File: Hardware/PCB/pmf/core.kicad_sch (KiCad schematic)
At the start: 44 parts, among them U1 AS3320, U2 TL072

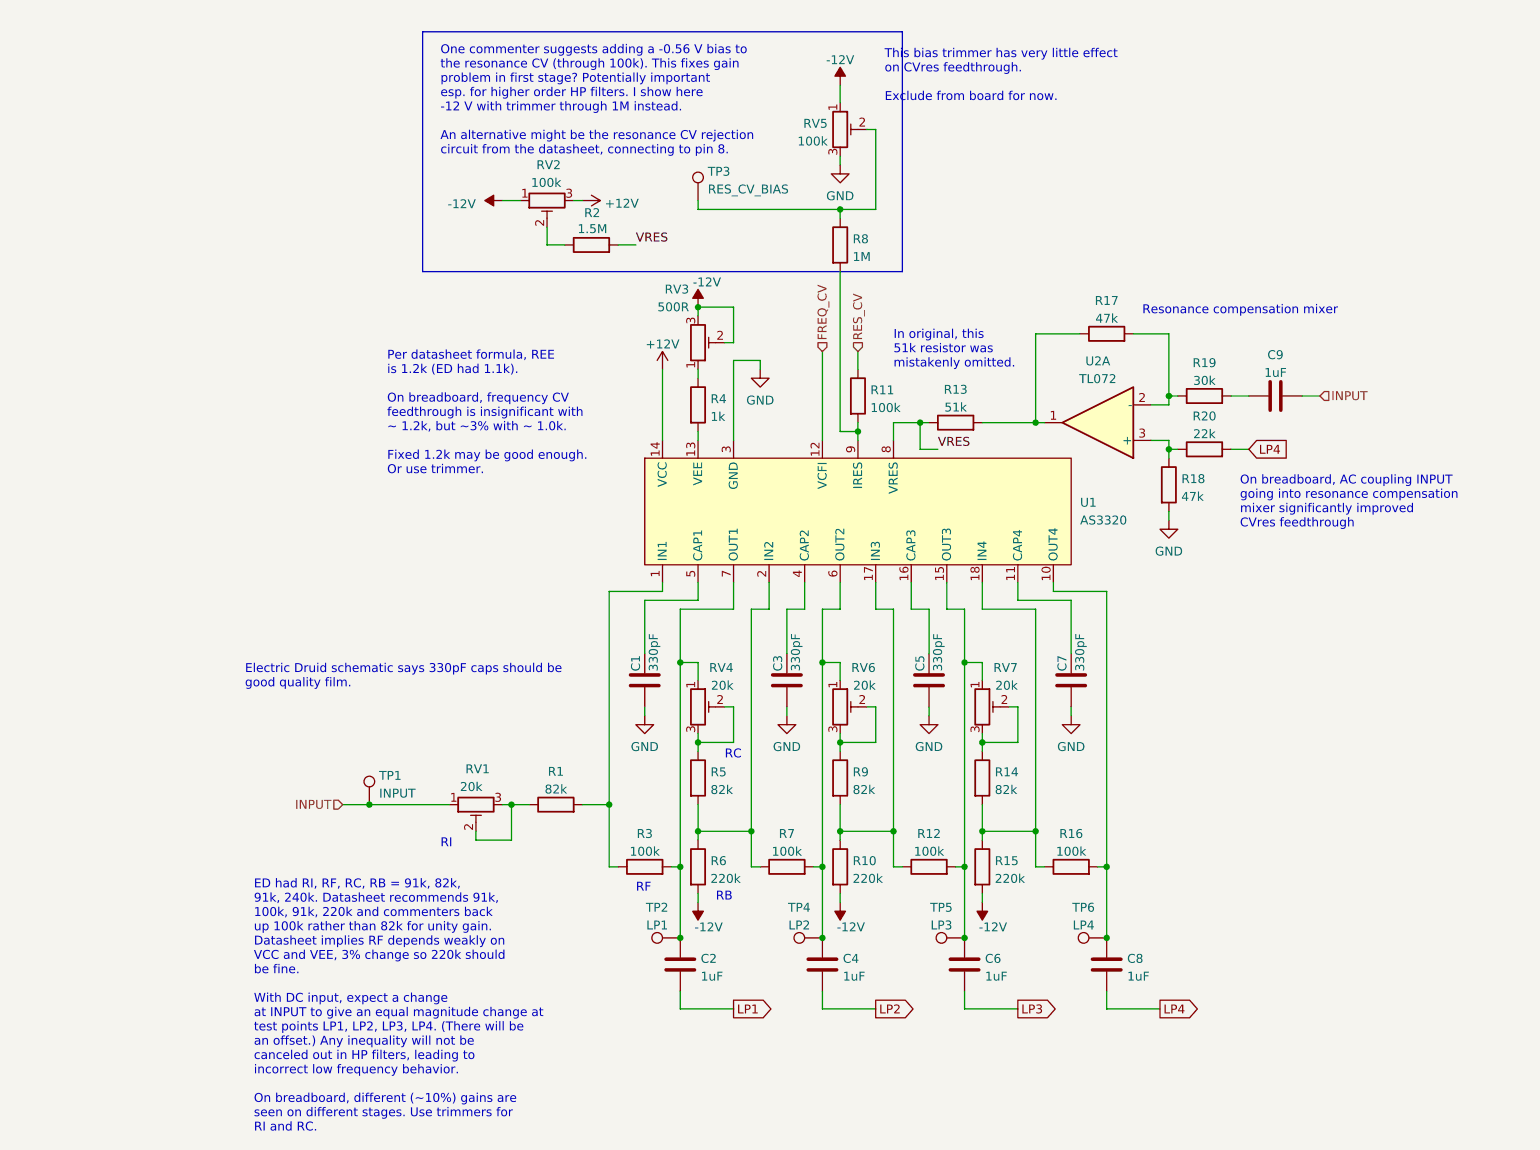
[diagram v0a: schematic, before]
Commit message: Reorganize filter core schematic
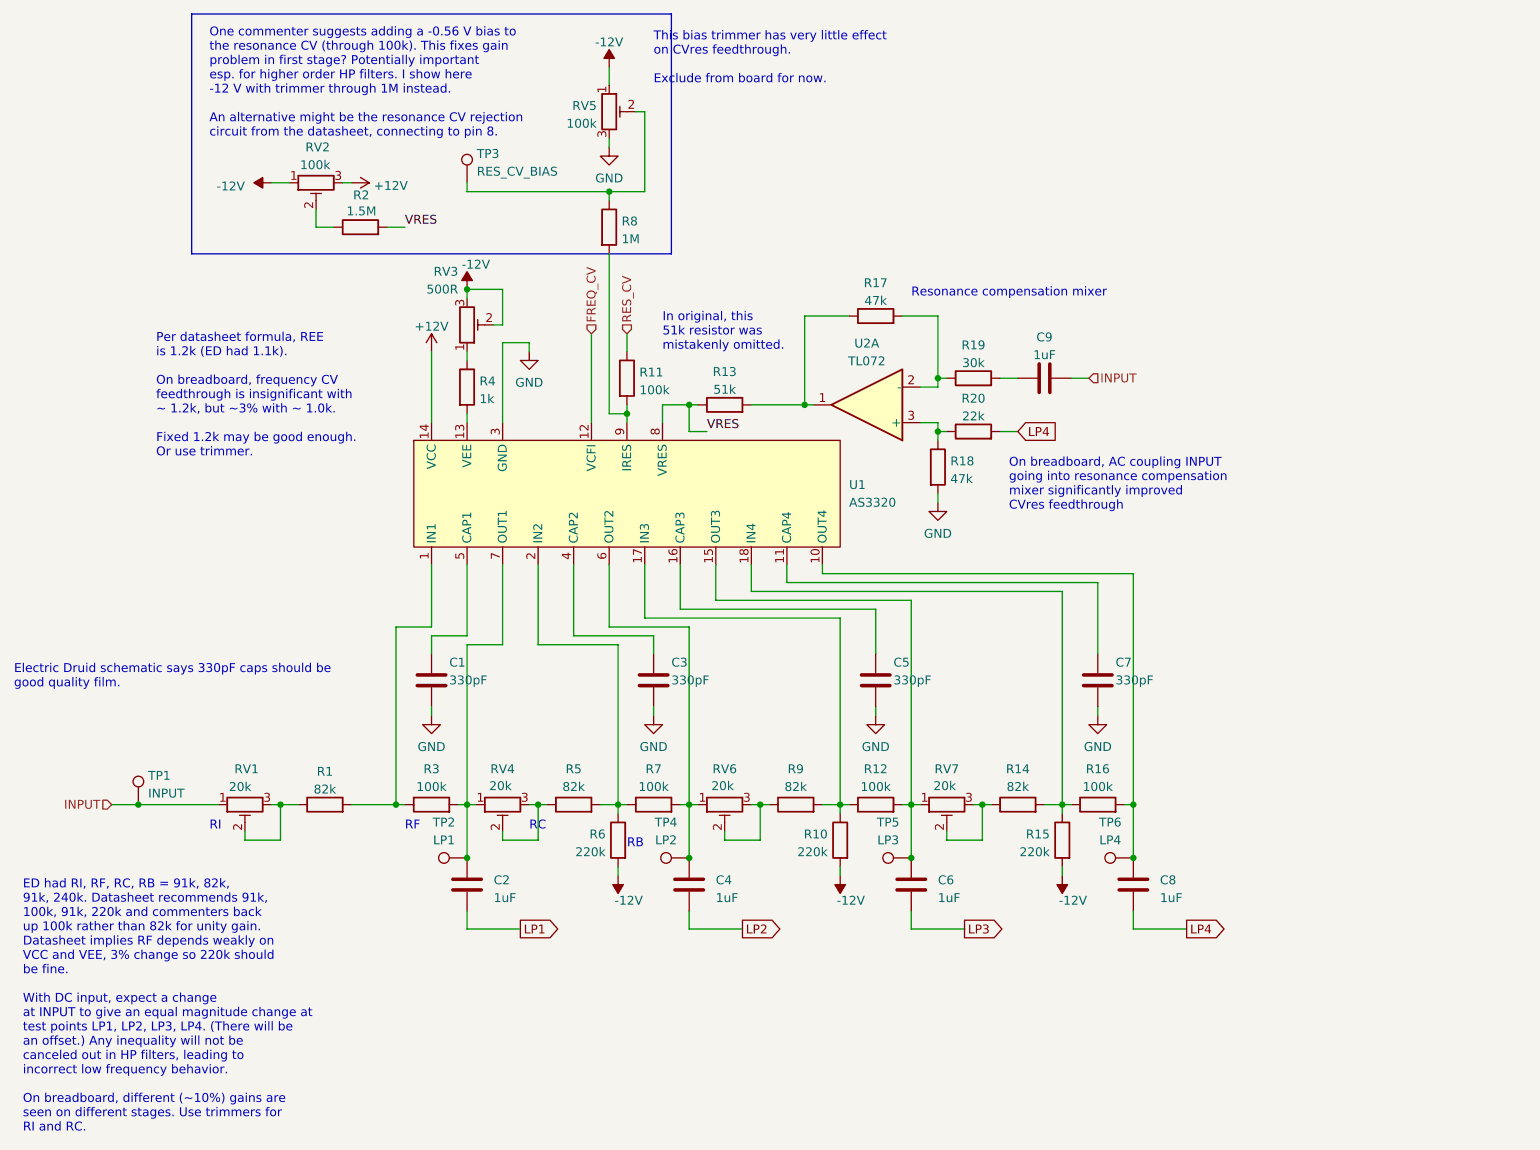
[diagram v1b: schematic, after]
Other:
- moved on the sheet: C1, C9, R1, R11, R13, R17, R18, R19, R2, R20, R4, R8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

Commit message: Rename libraries
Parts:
- C1, C3, C5, C7: footprint ao_tht:C_Rect_L7.2mm_W2.5mm_P5.00mm_FKS2_FKP2_MKS2_MKP2 -> AO_tht:C_Rect_L7.2mm_W2.5mm_P5.00mm_FKS2_FKP2_MKS2_MKP2; symbol ao_symbols:C -> AO_symbols:C
- C2, C4, C6, C8, C9: footprint ao_tht:C_Rect_L7.2mm_W7.2mm_P5.00mm_FKS2_FKP2_MKS2_MKP2 -> AO_tht:C_Rect_L7.2mm_W7.2mm_P5.00mm_FKS2_FKP2_MKS2_MKP2; symbol ao_symbols:C -> AO_symbols:C
- R1, R10, R11, R12, R13, R14, R15, R16, R17, R18, R19, R2, R20, R3, R4, R5, R6, R7, R8, R9: footprint ao_tht:R_Axial_DIN0207_L6.3mm_D2.5mm_P10.16mm_Horizontal -> AO_tht:R_Axial_DIN0207_L6.3mm_D2.5mm_P10.16mm_Horizontal; symbol ao_symbols:R -> AO_symbols:R
- RV1, RV2, RV3, RV4, RV5, RV6, RV7: footprint ao_tht:Potentiometer_Bourns_3296W_Vertical_standard -> AO_tht:Potentiometer_Bourns_3296W_Vertical_standard; symbol ao_symbols:R_POT_TRIM_3296W -> AO_symbols:R_POT_TRIM_3296W
- TP1, TP2, TP3, TP4, TP5, TP6: footprint ao_tht:TestPoint_THTPad_D1.5mm_Drill0.7mm -> AO_tht:TestPoint_THTPad_D1.5mm_Drill0.7mm; symbol ao_symbols:TestPoint -> AO_symbols:TestPoint
- U2: footprint ao_tht:DIP-8_W7.62mm_Socket_LongPads -> AO_tht:DIP-8_W7.62mm_Socket_LongPads; symbol ao_symbols:TL072 -> AO_symbols:TL072

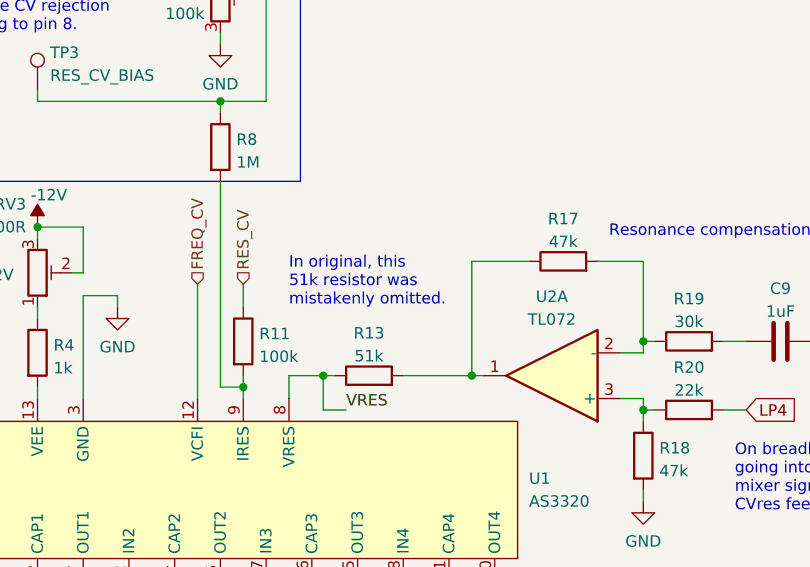
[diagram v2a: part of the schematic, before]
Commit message: Larger resistor for resonance input
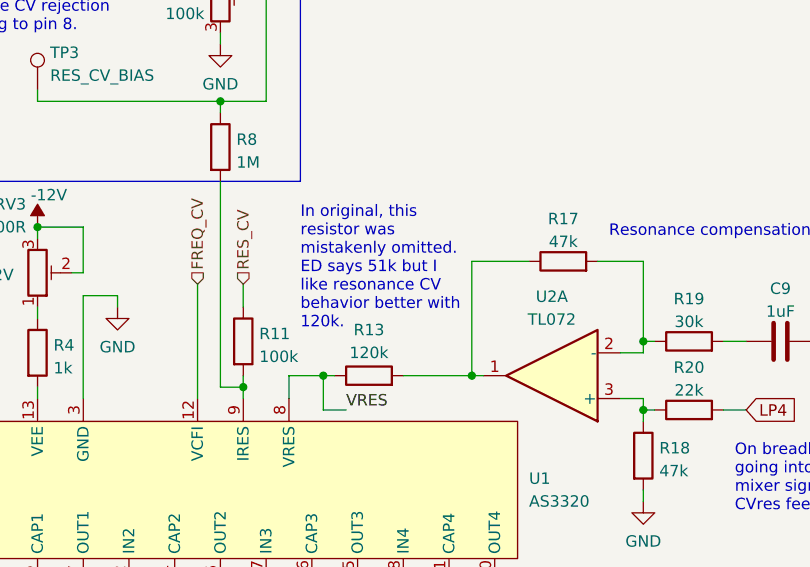
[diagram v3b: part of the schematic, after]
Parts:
- R13: value 51k -> 120k
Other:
- note added: "In original, this resistor was mistakenly omitted. ED says 51k but I like resonance CV behavior better with 120k."
- note removed: "In original, this 51k resistor was mistakenly omitted."
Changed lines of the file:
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@@
     (effects (font (size 1.27 1.27)) (justify left bottom))
   )
-  (text "In original, this\n51k resistor was\nmistakenly omitted."
-    (at 116.84 71.12 0)
+  (text "In original, this\nresistor was\nmistakenly omitted.\nED says 51k but I\nlike resonance CV\nbehavior better with\n120k."
+    (at 118.11 73.66 0)
     (effects (font (size 1.27 1.27)) (justify left bottom))
   )
@@
   (symbol (lib_id "AO_symbols:R") (at 125.73 78.74 90) (unit 1)
     (in_bom yes) (on_board yes) (dnp no) (fields_autoplaced)
-    (property "Reference" "R13" (at 125.73 74.0242 90)
-      (effects (font (size 1.27 1.27)))
-    )
-    (property "Value" "51k" (at 125.73 76.5611 90)
-      (effects (font (size 1.27 1.27)))
-    )
+    (property "Reference" "R13" (at 125.73 73.66 90)
+      (effects (font (size 1.27 1.27)))
+    )
+    (property "Value" "120k" (at 125.73 76.2 90)
+      (effects (font (size 1.27 1.27)))
+    )

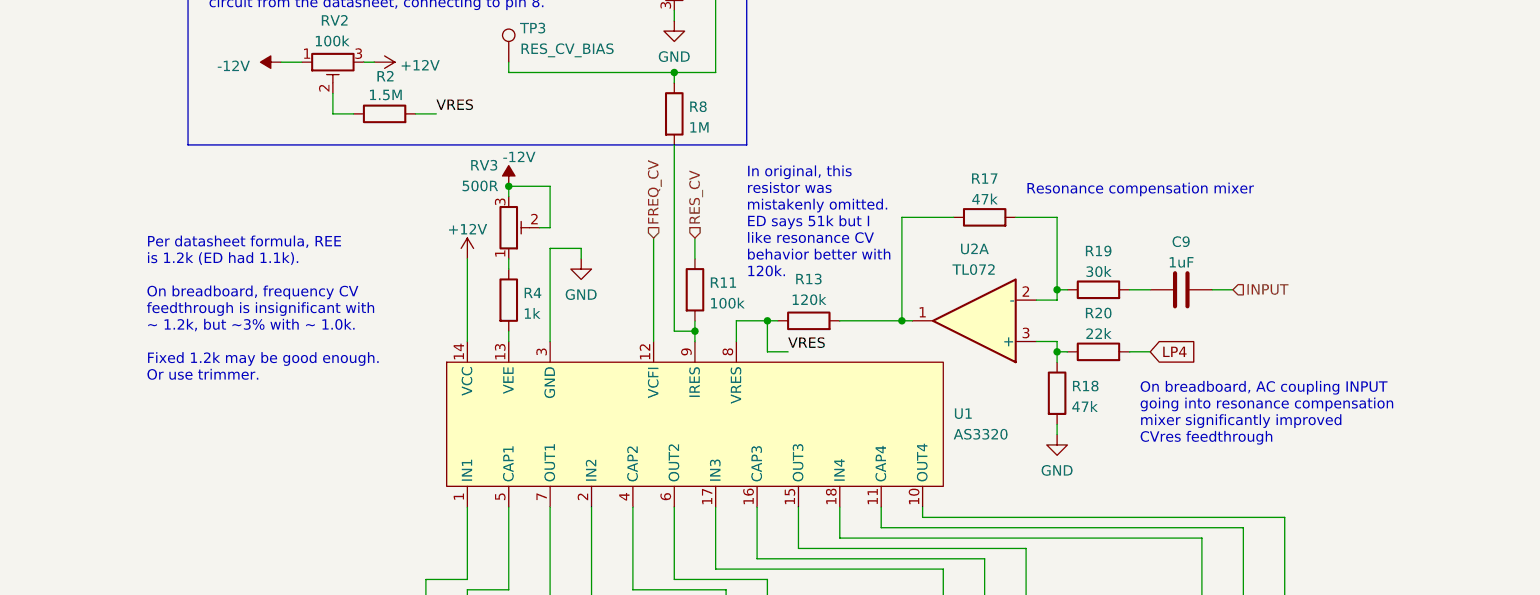
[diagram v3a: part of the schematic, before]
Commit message: Removed R_EE trimmer
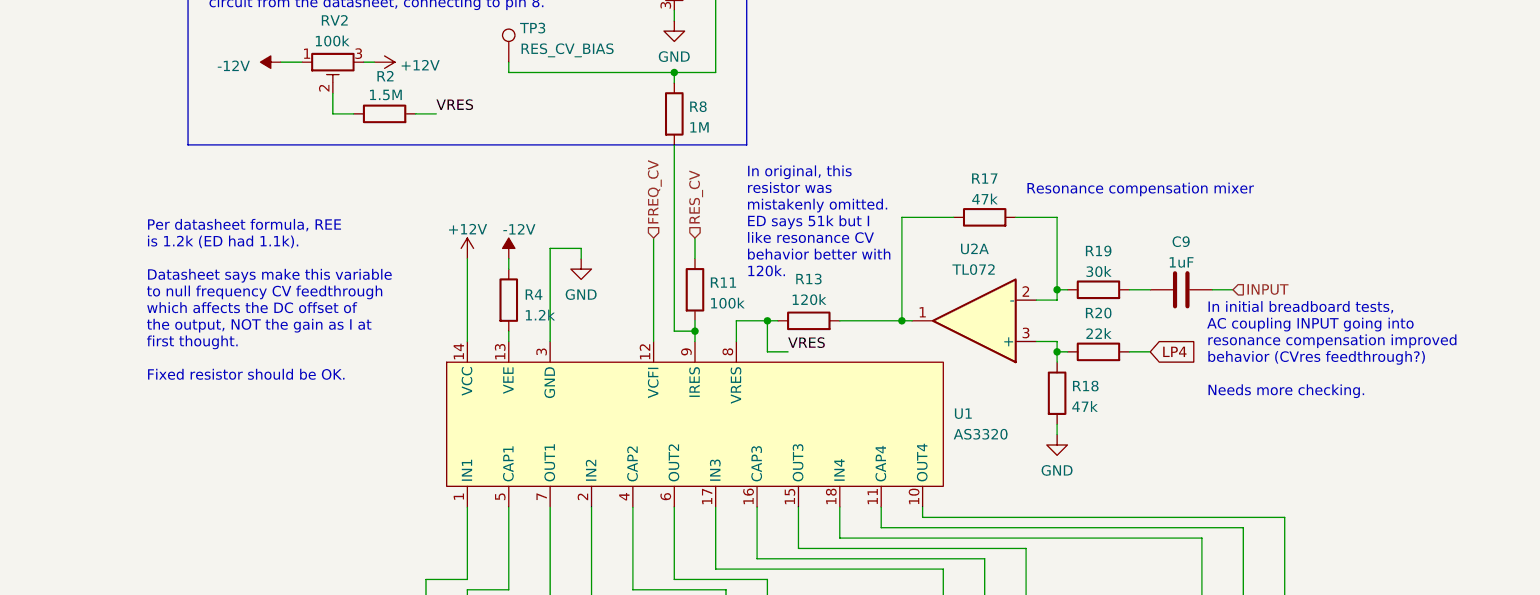
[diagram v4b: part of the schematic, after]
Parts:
- removed RV3: 500R, AO_tht:Potentiometer_Bourns_3296W_Vertical_standard, symbol AO_symbols:R_POT_TRIM_3296W
- R4: value 1k -> 1.2k
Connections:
- net -12V: now also R4.1
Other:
- note added: "In initial breadboard tests, AC coupling INPUT going into resonance compensation improved behavior (CVres feedthrough?) Needs more checking."
- note added: "Per datasheet formula, REE is 1.2k (ED had 1.1k). Datasheet says make this variable to null frequency CV feedthrough which affects the DC offset of the output, NOT the gain as I at first thought. Fixed resistor should be OK."
- note removed: "On breadboard, AC coupling INPUT going into resonance compensation mixer significantly improved CVres feedthrough"
- note removed: "Per datasheet formula, REE is 1.2k (ED had 1.1k). On breadboard, frequency CV feedthrough is insignificant with ~ 1.2k, but ~3% with ~ 1.0k. Fixed 1.2k may be good enough. Or use trimmer."
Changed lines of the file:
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@@
   (junction (at 111.76 80.01) (diameter 0) (color 0 0 0 0)
   )
-  (junction (at 88.9 62.23) (diameter 0) (color 0 0 0 0)
-  )
   (junction (at 78.74 135.89) (diameter 0) (color 0 0 0 0)
   )
@@
     (stroke (width 0) (type default))
   )
-  (wire (pts (xy 88.9 63.5) (xy 88.9 62.23))
-    (stroke (width 0) (type default))
-  )
   (wire (pts (xy 78.74 135.89) (xy 80.01 135.89))
     (stroke (width 0) (type default))
@@
     (stroke (width 0) (type default))
   )
-  (wire (pts (xy 93.98 62.23) (xy 93.98 67.31))
-    (stroke (width 0) (type default))
-  )
   (wire (pts (xy 83.82 110.49) (xy 78.74 110.49))
     (stroke (width 0) (type default))
@@
     (stroke (width 0) (type default))
   )
-  (wire (pts (xy 88.9 62.23) (xy 93.98 62.23))
-    (stroke (width 0) (type default))
-  )
   (wire (pts (xy 93.98 139.7) (xy 93.98 140.97))
     (stroke (width 0) (type default))
@@
   )
   (wire (pts (xy 120.65 153.67) (xy 128.27 153.67))
-    (stroke (width 0) (type default))
-  )
-  (wire (pts (xy 92.71 67.31) (xy 93.98 67.31))
     (stroke (width 0) (type default))
   )
@@
     (effects (font (size 1.27 1.27)) (justify left bottom))
   )
-  (text "On breadboard, AC coupling INPUT\ngoing into resonance compensation\nmixer significantly improved\nCVres feedthrough"
-    (at 166.37 93.98 0)
+  (text "In initial breadboard tests, \nAC coupling INPUT going into \nresonance compensation improved\nbehavior (CVres feedthrough?)\n\nNeeds more checking.\n"
+    (at 174.625 88.265 0)
     (effects (font (size 1.27 1.27)) (justify left bottom))
   )
@@
     (effects (font (size 1.27 1.27)) (justify left bottom))
   )
-  (text "Per datasheet formula, REE\nis 1.2k (ED had 1.1k).\n\nOn breadboard, frequency CV\nfeedthrough is insignificant with\n~ 1.2k, but ~3% with ~ 1.0k. \n\nFixed 1.2k may be good enough. \nOr use trimmer."
+  (text "Per datasheet formula, REE\nis 1.2k (ED had 1.1k).\n\nDatasheet says make this variable\nto null frequency CV feedthrough\nwhich affects the DC offset of \nthe output, NOT the gain as I at\nfirst thought. \n\nFixed resistor should be OK."
     (at 44.45 86.36 0)
     (effects (font (size 1.27 1.27)) (justify left bottom))
@@
     )
   )
-  (symbol (lib_id "AO_symbols:R_POT_TRIM_3296W") (at 88.9 67.31 0) (mirror x) (unit 1)
-    (in_bom yes) (on_board yes) (dnp no)
-    (property "Reference" "RV3" (at 87.63 59.6931 0)
-      (effects (font (size 1.27 1.27)) (justify right))
-    )
-    (property "Value" "500R" (at 87.63 62.23 0)
-      (effects (font (size 1.27 1.27)) (justify right))
-    )
-    (property "Footprint" "AO_tht:Potentiometer_Bourns_3296W_Vertical_standard" (at 88.9 67.31 0)
-      (effects (font (size 1.27 1.27)) hide)
-    )
-    (property "Datasheet" "~" (at 88.9 67.31 0)
-      (effects (font (size 1.27 1.27)) hide)
-    )
-    (property "Vendor" "Tayda" (at 88.9 67.31 0)
-      (effects (font (size 1.27 1.27)) hide)
-    )
-    (pin "1")
-    (pin "2")
-    (pin "3")
-    (instances
-      (project "pmf"
-        (path "/1fce46f5-2003-4c7e-915f-b9b7dfc679d7/2085c2ec-887c-4fdb-9d07-ac0ffcad932c"
-          (reference "RV3") (unit 1)
-        )
-      )
-    )
-  )
   (symbol (lib_id "AO_symbols:C") (at 88.9 147.32 0) (unit 1)
     (in_bom yes) (on_board yes) (dnp no) (fields_autoplaced)
@@
   )
   (symbol (lib_id "AO_symbols:R") (at 88.9 76.2 0) (unit 1)
-    (in_bom yes) (on_board yes) (dnp no) (fields_autoplaced)
-    (property "Reference" "R4" (at 90.678 75.3653 0)
-      (effects (font (size 1.27 1.27)) (justify left))
-    )
-    (property "Value" "1k" (at 90.678 77.9022 0)
+    (in_bom yes) (on_board yes) (dnp no)
+    (property "Reference" "R4" (at 90.805 75.565 0)
+      (effects (font (size 1.27 1.27)) (justify left))
+    )
+    (property "Value" "1.2k" (at 90.805 78.105 0)
       (effects (font (size 1.27 1.27)) (justify left))
     )
@@
     )
   )
-  (symbol (lib_id "power:-12V") (at 88.9 62.23 0) (unit 1)
+  (symbol (lib_id "power:-12V") (at 88.9 71.12 0) (unit 1)
     (in_bom yes) (on_board yes) (dnp no)
-    (property "Reference" "#PWR05" (at 88.9 59.69 0)
-      (effects (font (size 1.27 1.27)) hide)
-    )
-    (property "Value" "-12V" (at 90.17 58.674 0)
-      (effects (font (size 1.27 1.27)))
-    )
-    (property "Footprint" "" (at 88.9 62.23 0)
-      (effects (font (size 1.27 1.27)) hide)
-    )
-    (property "Datasheet" "" (at 88.9 62.23 0)
-      (effects (font (size 1.27 1.27)) hide)
-    )
+    (property "Reference" "#PWR05" (at 88.9 68.58 0)
+      (effects (font (size 1.27 1.27)) hide)
+    )
+    (property "Value" "-12V" (at 90.17 67.564 0)
+      (effects (font (size 1.27 1.27)))
+    )
+    (property "Footprint" "" (at 88.9 71.12 0)
+      (effects (font (size 1.27 1.27)) hide)
+    )
+    (property "Datasheet" "" (at 88.9 71.12 0)
+      (effects (font (size 1.27 1.27)) hide)
+    )
